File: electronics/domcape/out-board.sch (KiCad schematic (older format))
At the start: 6 parts, among them IC1 PC817, P1 CONN_01X03, P2 CONN_01X04, Q1 IRF540N

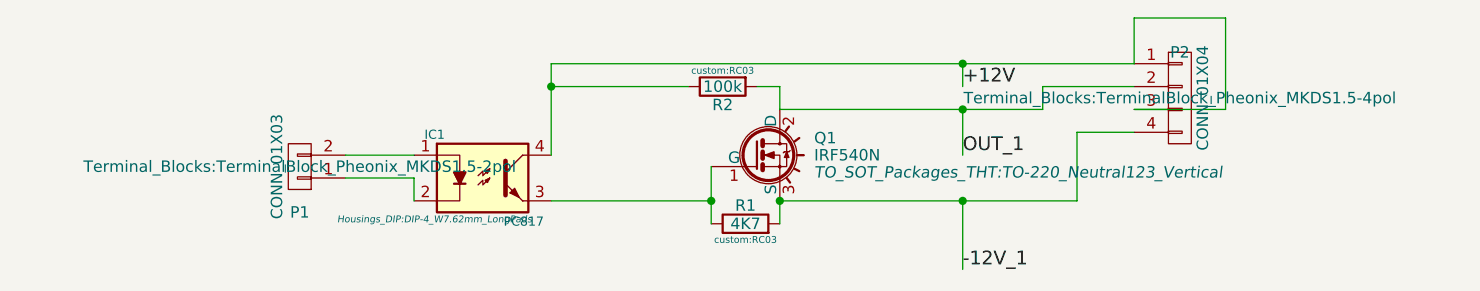
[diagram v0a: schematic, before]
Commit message: out-board circuit corrections
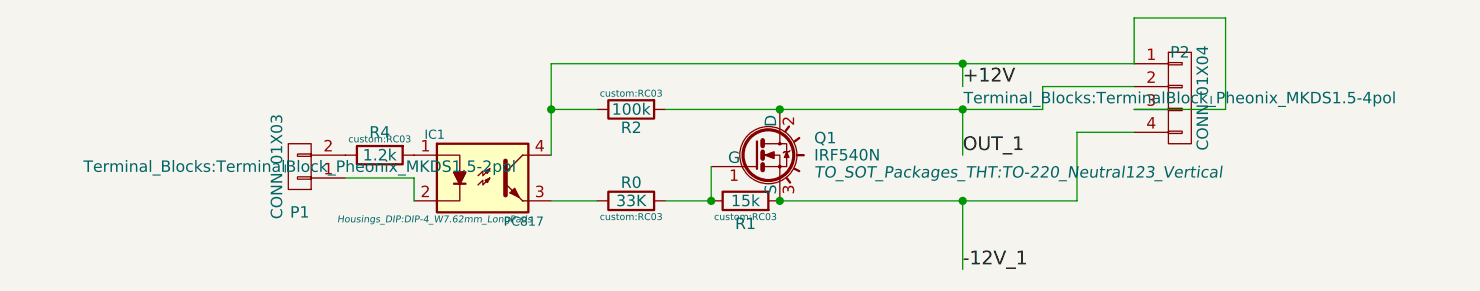
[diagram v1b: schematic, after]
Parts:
- added R0: 33K, custom:RC03, symbol R
- added R4: 1.2k, custom:RC03, symbol R
- R1: value 4K7 -> 15k
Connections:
- net at IC1.1: now also R4.2; no longer P1.2 (P2)
- net at Q1.1 (G), R1.1: now also R0.2; no longer IC1.3
- new net: IC1.3, R0.1
- new net: P1.2 (P2), R4.1
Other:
- moved on the sheet: R1, R2
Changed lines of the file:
@@
 L R R2
 U 1 1 55BF39C7
-P 5700 3300
-F 0 "R2" V 5780 3300 50  0000 C CNN
-F 1 "100k" V 5700 3300 50  0000 C CNN
-F 2 "custom:RC03" V 5630 3300 30  0000 C CNN
-F 3 "" H 5700 3300 30  0000 C CNN
-	1    5700 3300
+P 5300 3400
+F 0 "R2" V 5380 3400 50  0000 C CNN
+F 1 "100k" V 5300 3400 50  0000 C CNN
+F 2 "custom:RC03" V 5230 3400 30  0000 C CNN
+F 3 "" H 5300 3400 30  0000 C CNN
+	1    5300 3400
 	0    -1   1    0
 $EndComp
@@
 L R R1
 U 1 1 55BF62EA
-P 5800 3900
-F 0 "R1" V 5880 3900 50  0000 C CNN
-F 1 "4K7" V 5800 3900 50  0000 C CNN
-F 2 "custom:RC03" V 5730 3900 30  0000 C CNN
-F 3 "" H 5800 3900 30  0000 C CNN
-	1    5800 3900
+P 5800 3800
+F 0 "R1" V 5700 3800 50  0000 C CNN
+F 1 "15k" V 5800 3800 50  0000 C CNN
+F 2 "custom:RC03" V 5730 3800 30  0000 C CNN
+F 3 "" H 5800 3800 30  0000 C CNN
+	1    5800 3800
 	0    -1   -1   0
 $EndComp
@@
 Connection ~ 6750 3400
 Wire Wire Line
-	5950 3400 7100 3400
-Wire Wire Line
-	4050 3600 4350 3600
+	5450 3400 7100 3400
 Wire Wire Line
 	5950 3800 7250 3800
@@
 Wire Wire Line
 	4950 3200 4950 3600
-Wire Wire Line
-	5650 3900 5650 3650
 $Comp
 L IRF540N Q1
@@
 	1    0    0    -1
 $EndComp
-Wire Wire Line
-	4950 3800 5650 3800
 Connection ~ 5650 3800
-Wire Wire Line
-	5550 3300 4950 3300
-Wire Wire Line
-	5850 3300 5950 3300
-Wire Wire Line
-	5950 3300 5950 3400
-Wire Wire Line
-	5950 3800 5950 3900
 Connection ~ 5950 3800
 $Comp
@@
 Wire Wire Line
 	4950 3200 7500 3200
-Connection ~ 4950 3300
 Connection ~ 6750 3800
 Wire Wire Line
@@
 Wire Wire Line
 	7900 3400 7500 3400
+$Comp
+L R R0
+U 1 1 59BB0113
+P 5300 3800
+F 0 "R0" V 5380 3800 50  0000 C CNN
+F 1 "33K" V 5300 3800 50  0000 C CNN
+F 2 "custom:RC03" V 5230 3800 30  0000 C CNN
+F 3 "" H 5300 3800 30  0000 C CNN
+	1    5300 3800
+	0    -1   -1   0
+$EndComp
+Wire Wire Line
+	4950 3800 5150 3800
+Wire Wire Line
+	5450 3800 5650 3800
+Wire Wire Line
+	5650 3800 5650 3650
+Connection ~ 5950 3400
+Wire Wire Line
+	5150 3400 4950 3400
+Connection ~ 4950 3400
+$Comp
+L R R4
+U 1 1 59BB097A
+P 4200 3600
+F 0 "R4" V 4100 3600 50  0000 C CNN
+F 1 "1.2k" V 4200 3600 50  0000 C CNN
+F 2 "custom:RC03" V 4130 3600 30  0000 C CNN
+F 3 "" H 4200 3600 30  0000 C CNN
+	1    4200 3600
+	0    -1   1    0
+$EndComp
 $EndSCHEMATC
